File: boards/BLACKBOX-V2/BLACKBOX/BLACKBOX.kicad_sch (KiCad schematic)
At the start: 23 parts, among them J1 Micro_SD_Card, J2 Conn_01x02_Female, U2 Adafruit-BNO085, U4 MS5611-01BA

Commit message: Preliminary layout complete
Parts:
- removed D1: BLUE, symbol Simulation_SPICE:DIODE
- removed D2: RED, symbol Simulation_SPICE:DIODE
- added D103: BLUE, LED_SMD:LED_0805_2012Metric, symbol Device:LED
- added D104: RED, LED_SMD:LED_0805_2012Metric, symbol Device:LED
- R103: renamed from R5; value 10kΩ -> 10k
- R104: renamed from R6; value 10kΩ -> 10k
- R105: renamed from R3; footprint (none) -> Resistor_SMD:R_0805_2012Metric
- R106: renamed from R4; footprint (none) -> Resistor_SMD:R_0805_2012Metric
- gave numbers to parts that had none: 4
- renumbered A1 to A101, C2 to C101, C6 to C104, D3 to D101, D4 to D102, J1 to J101, J2 to J102, JP1 to JP102, JP3 to JP103, R1 to R101, R2 to R102, U2 to U101, U4 to U103
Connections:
- net 3V3 is gone; now on net +3V3: JP101.1
- net KX122_CS is gone; now on net KX_CS: U102.10 (~{CS})
- net KX122_INT1 is gone; now on net KX_INT1: U102.5 (INT1)
- net KX122_INT2 is gone; now on net KX_INT2: U102.6 (INT2)
- net SNS_SPI_MISO is gone; now on net MISO: U102.1 (SDO/ADDR)
- net SNS_SPI_MOSI is gone; now on net MOSI: U102.2 (SDI/SDA)
- net SNS_SPI_SCK is gone; now on net SCK: U102.12 (SCLK/SCL)
- net LED2: now also D103.2 (A)
- net LED3: now also D104.2 (A)
- net at R106.1: now also D104.1 (K)
- net at R105.1: now also D103.1 (K)
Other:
- note added: "LEDs"
- moved on the sheet: D101, D102, R103, R104, R105, R106

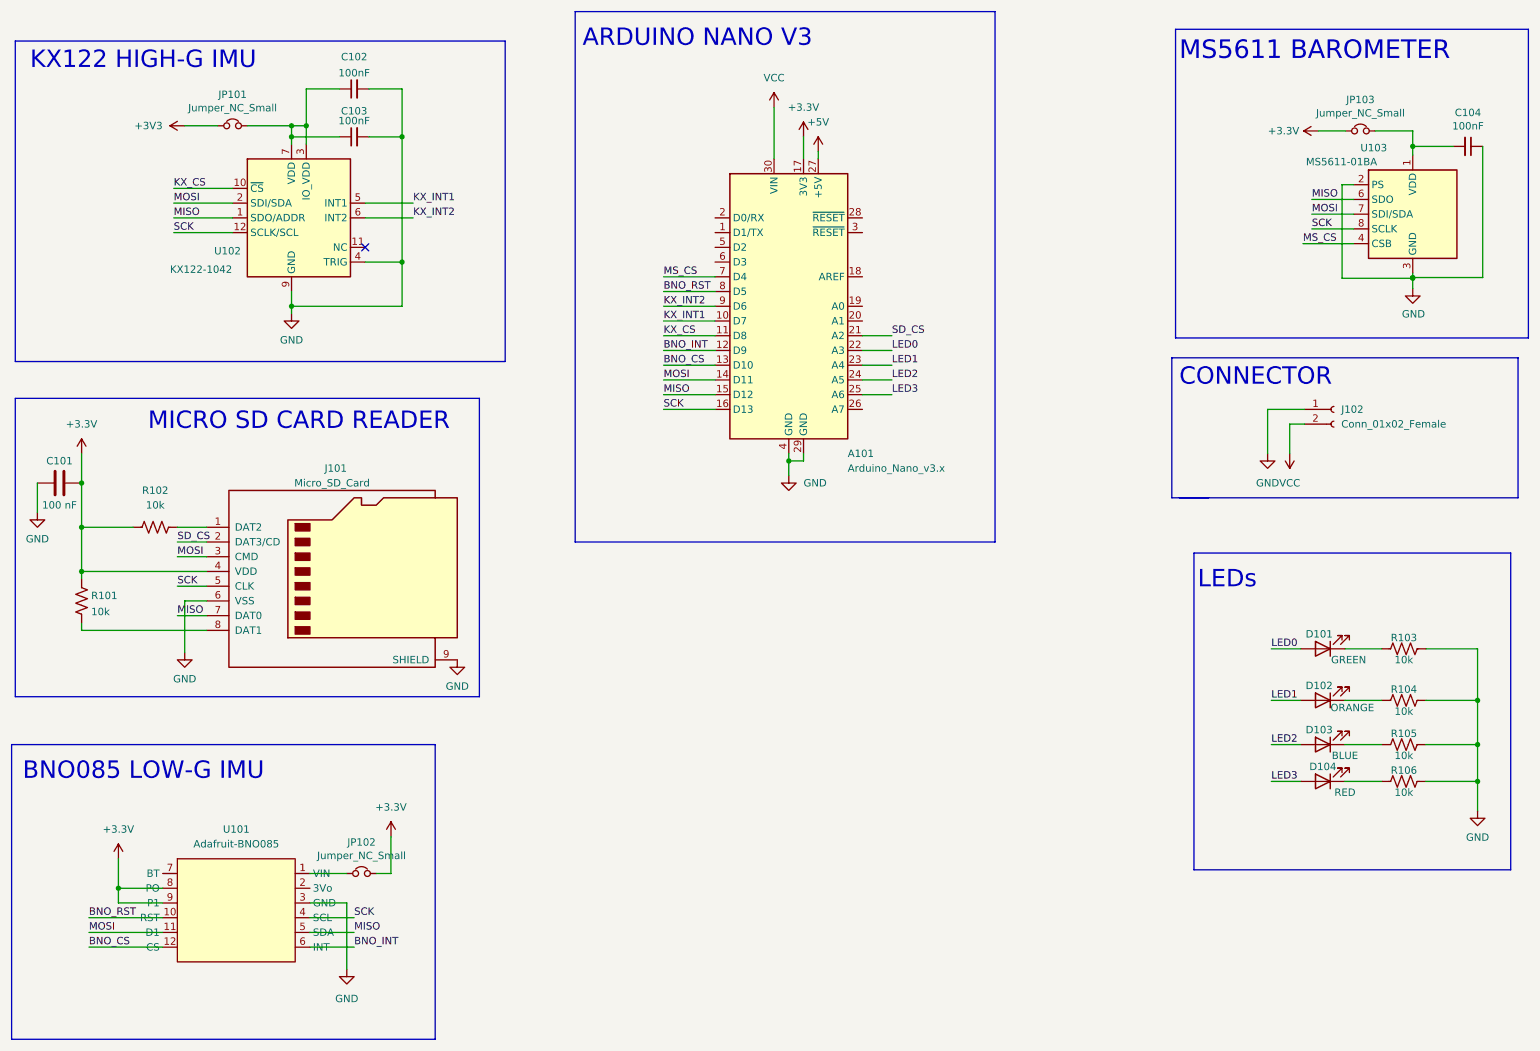
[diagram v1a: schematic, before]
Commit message: finished blackbox routing;
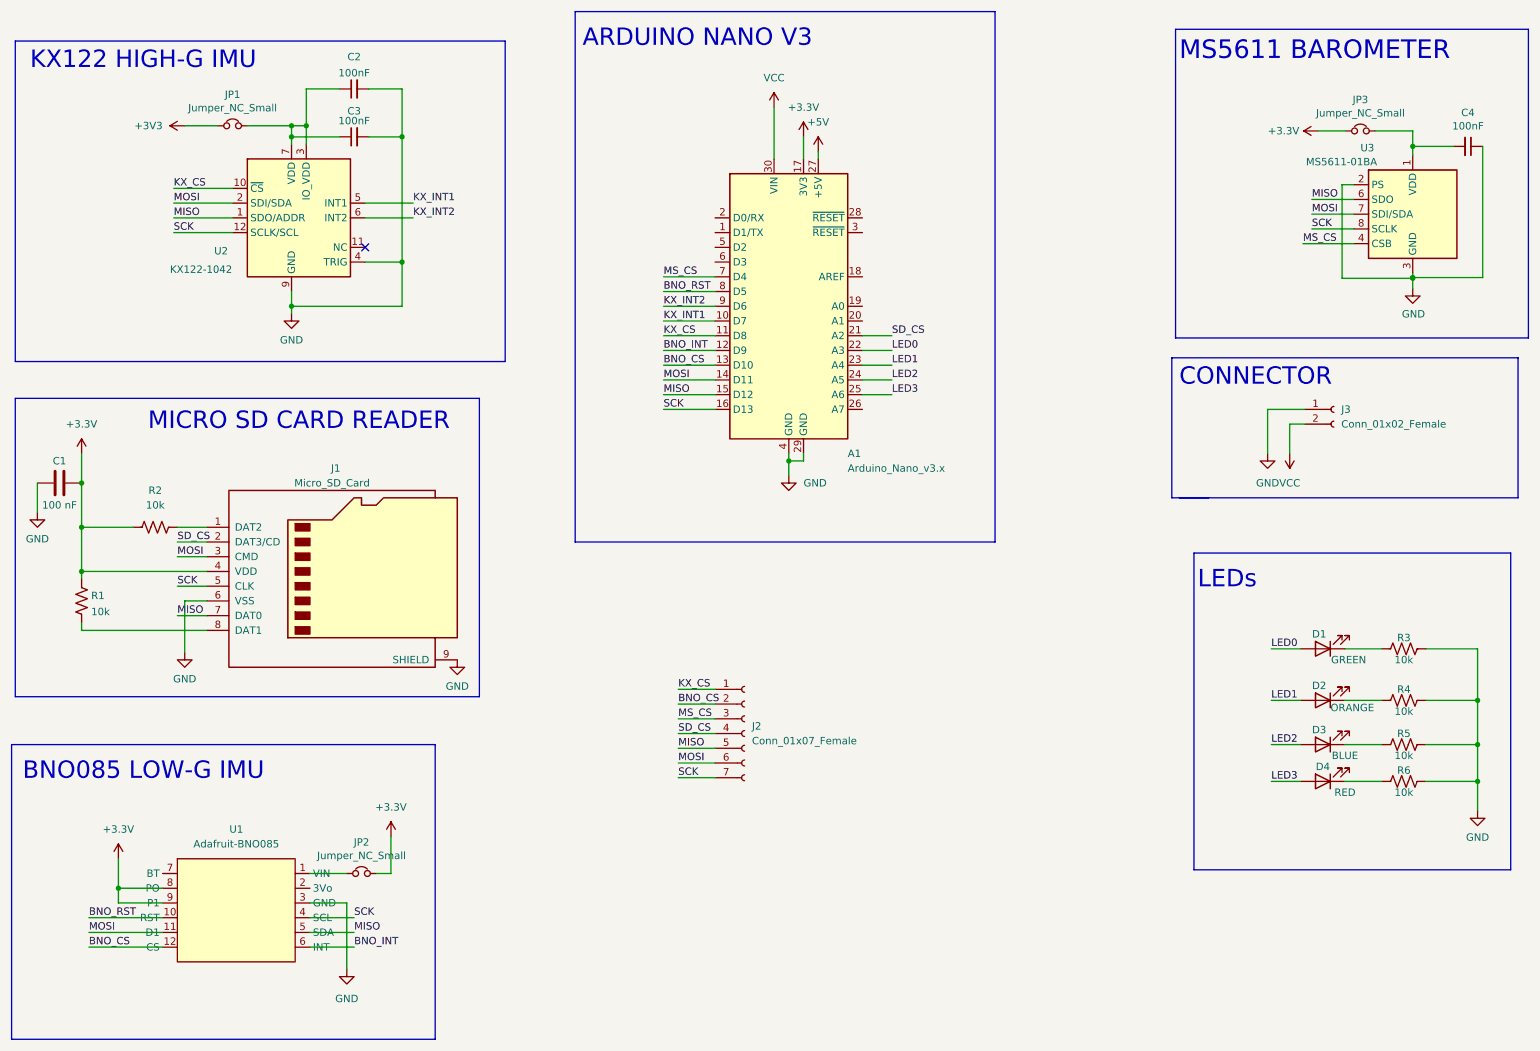
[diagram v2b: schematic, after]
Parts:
- added J2: Conn_01x07_Female, Connector_PinHeader_2.54mm:PinHeader_1x07_P2.54mm_Vertical, symbol Connector:Conn_01x07_Female
- renumbered A101 to A1, C101 to C1, C102 to C2, C103 to C3, C104 to C4, D101 to D1, D102 to D2, D103 to D3, D104 to D4, J101 to J1, J102 to J3, JP101 to JP1, JP102 to JP2, JP103 to JP3, R101 to R1, R102 to R2, R103 to R3, R104 to R4, R105 to R5, R106 to R6, U101 to U1, U102 to U2, U103 to U3
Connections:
- net BNO_CS: now also J2.2 (Pin_2)
- net KX_CS: now also J2.1 (Pin_1)
- net MISO: now also J2.5 (Pin_5)
- net MOSI: now also J2.6 (Pin_6)
- net MS_CS: now also J2.3 (Pin_3)
- net SCK: now also J2.7 (Pin_7)
- net SD_CS: now also J2.4 (Pin_4)

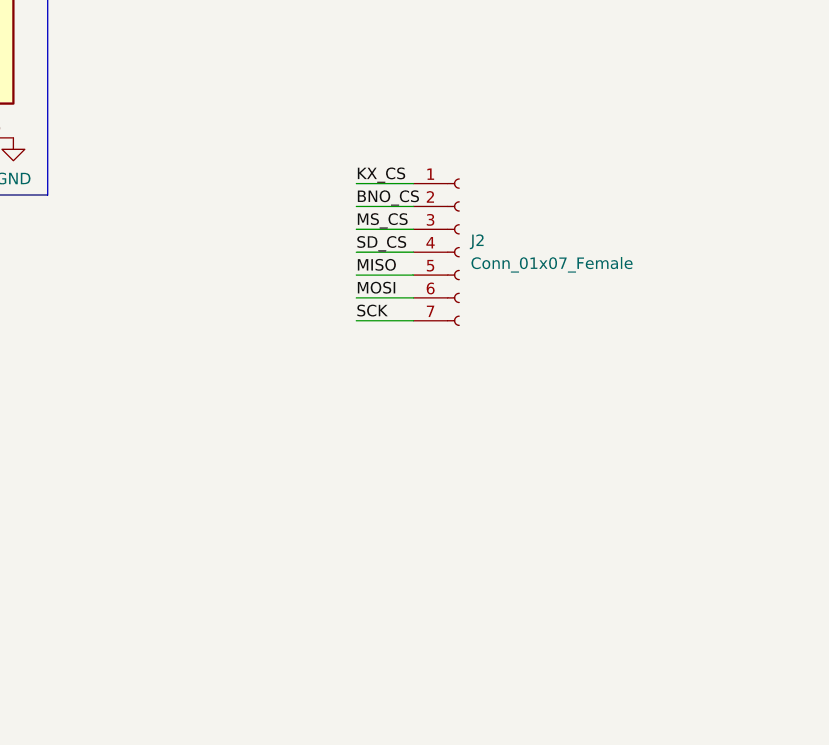
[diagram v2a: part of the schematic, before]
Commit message: Updated schematic for better readability
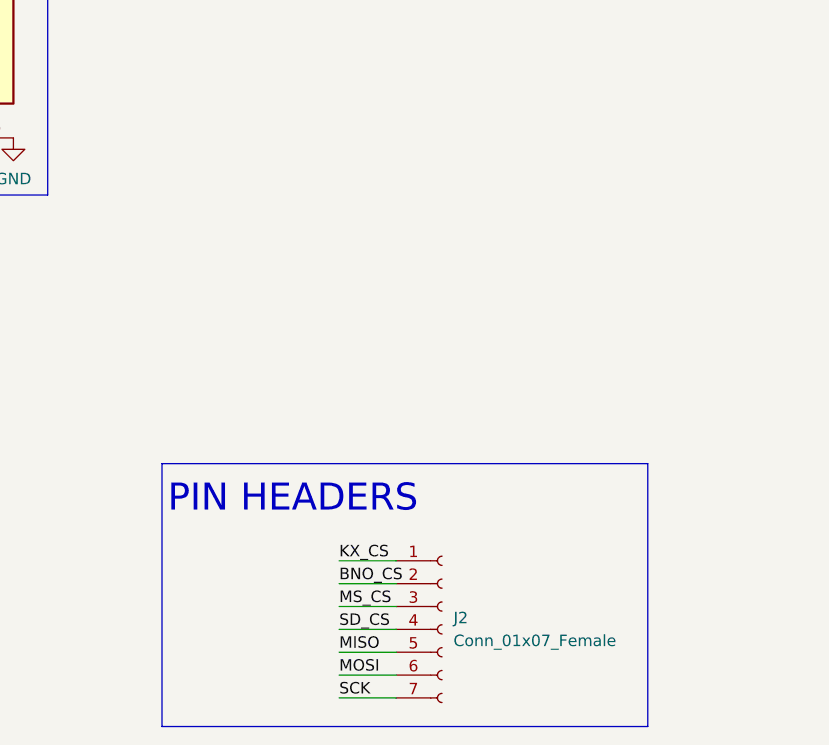
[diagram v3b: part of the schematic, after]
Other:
- note added: "PIN HEADERS"
- moved on the sheet: J2
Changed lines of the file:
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@@
     (stroke (width 0) (type default) (color 0 0 0 0))
   )
-  (wire (pts (xy 134.62 144.78) (xy 140.97 144.78))
+  (wire (pts (xy 132.715 186.69) (xy 139.065 186.69))
     (stroke (width 0) (type default) (color 0 0 0 0))
   )
@@
     (stroke (width 0) (type default) (color 0 0 0 0))
   )
-  (wire (pts (xy 134.62 137.16) (xy 140.97 137.16))
+  (wire (pts (xy 132.715 179.07) (xy 139.065 179.07))
     (stroke (width 0) (type default) (color 0 0 0 0))
   )
@@
     (stroke (width 0) (type default) (color 0 0 0 0))
   )
-  (wire (pts (xy 134.62 132.08) (xy 140.97 132.08))
-    (stroke (width 0) (type default) (color 0 0 0 0))
-  )
-  (wire (pts (xy 134.62 142.24) (xy 140.97 142.24))
+  (wire (pts (xy 132.715 173.99) (xy 139.065 173.99))
+    (stroke (width 0) (type default) (color 0 0 0 0))
+  )
+  (wire (pts (xy 132.715 184.15) (xy 139.065 184.15))
     (stroke (width 0) (type default) (color 0 0 0 0))
   )
@@
     (stroke (width 0) (type default) (color 0 0 0 0))
   )
-  (wire (pts (xy 134.62 139.7) (xy 140.97 139.7))
+  (wire (pts (xy 132.715 181.61) (xy 139.065 181.61))
     (stroke (width 0) (type default) (color 0 0 0 0))
   )
@@
     (stroke (width 0) (type default) (color 0 0 0 0))
   )
+  (polyline (pts (xy 113.03 160.655) (xy 167.005 160.655))
+    (stroke (width 0) (type default) (color 0 0 0 0))
+  )
   (polyline (pts (xy 92.71 189.865) (xy 19.685 189.865))
     (stroke (width 0) (type default) (color 0 0 0 0))
   )
+  (polyline (pts (xy 113.03 189.865) (xy 167.005 189.865))
+    (stroke (width 0) (type default) (color 0 0 0 0))
+  )
   (wire (pts (xy 67.945 60.96) (xy 67.945 63.5))
     (stroke (width 0) (type default) (color 0 0 0 0))
@@
     (stroke (width 0) (type default) (color 0 0 0 0))
   )
+  (polyline (pts (xy 167.005 189.865) (xy 167.005 160.655))
+    (stroke (width 0) (type default) (color 0 0 0 0))
+  )
   (wire (pts (xy 261.239 57.785) (xy 261.239 58.547))
     (stroke (width 0) (type default) (color 0 0 0 0))
@@
     (stroke (width 0) (type default) (color 0 0 0 0))
   )
+  (polyline (pts (xy 113.03 160.655) (xy 113.03 189.865))
+    (stroke (width 0) (type default) (color 0 0 0 0))
+  )
   (wire (pts (xy 45.72 163.83) (xy 38.1 163.83))
     (stroke (width 0) (type default) (color 0 0 0 0))
@@
     (stroke (width 0) (type default) (color 0 0 0 0))
   )
-  (wire (pts (xy 134.62 134.62) (xy 140.97 134.62))
+  (wire (pts (xy 132.715 176.53) (xy 139.065 176.53))
     (stroke (width 0) (type default) (color 0 0 0 0))
   )
@@
     (stroke (width 0) (type default) (color 0 0 0 0))
   )
-  (wire (pts (xy 134.62 129.54) (xy 140.97 129.54))
+  (wire (pts (xy 132.715 171.45) (xy 139.065 171.45))
     (stroke (width 0) (type default) (color 0 0 0 0))
   )
@@
     (effects (font (size 3.2004 3.2004)) (justify left bottom))
   )
+  (text "PIN HEADERS" (at 113.665 166.37 0)
+    (effects (font (size 3 3)) (justify left bottom))
+  )
   (label "MS_CS" (at 132.08 58.42 0)
     (effects (font (size 1.27 1.27)) (justify left bottom))
@@
     (effects (font (size 1.27 1.27)) (justify left bottom))
   )
-  (label "SCK" (at 134.62 144.78 0)
+  (label "SCK" (at 132.715 186.69 0)
     (effects (font (size 1.27 1.27)) (justify left bottom))
   )
@@
     (effects (font (size 1.27 1.27)) (justify left bottom))
   )
-  (label "MISO" (at 134.62 139.7 0)
+  (label "MISO" (at 132.715 181.61 0)
     (effects (font (size 1.27 1.27)) (justify left bottom))
   )
@@
     (effects (font (size 1.27 1.27)) (justify left bottom))
   )
-  (label "MS_CS" (at 134.62 134.62 0)
+  (label "MS_CS" (at 132.715 176.53 0)
     (effects (font (size 1.27 1.27)) (justify left bottom))
   )
@@
     (effects (font (size 1.27 1.27)) (justify left bottom))
   )
-  (label "KX_CS" (at 134.62 129.54 0)
+  (label "KX_CS" (at 132.715 171.45 0)
     (effects (font (size 1.27 1.27)) (justify left bottom))
   )
@@
     (effects (font (size 1.27 1.27)) (justify left bottom))
   )
-  (label "MOSI" (at 134.62 142.24 0)
+  (label "MOSI" (at 132.715 184.15 0)
     (effects (font (size 1.27 1.27)) (justify left bottom))
   )
@@
     (effects (font (size 1.27 1.27)) (justify left bottom))
   )
-  (label "SD_CS" (at 134.62 137.16 0)
+  (label "SD_CS" (at 132.715 179.07 0)
     (effects (font (size 1.27 1.27)) (justify left bottom))
   )
@@
     (effects (font (size 1.27 1.27)) (justify left bottom))
   )
-  (label "BNO_CS" (at 134.62 132.08 0)
+  (label "BNO_CS" (at 132.715 173.99 0)
     (effects (font (size 1.27 1.27)) (justify left bottom))
   )
@@
     (pin "2")
   )
-  (symbol (lib_id "Connector:Conn_01x07_Female") (at 146.05 137.16 0) (unit 1)
+  (symbol (lib_id "Connector:Conn_01x07_Female") (at 144.145 179.07 0) (unit 1)
     (in_bom yes) (on_board yes) (fields_autoplaced)
-    (property "Reference" "J2" (id 0) (at 147.32 135.8899 0)
+    (property "Reference" "J2" (id 0) (at 145.415 177.7999 0)
       (effects (font (size 1.27 1.27)) (justify left))
     )
-    (property "Value" "Conn_01x07_Female" (id 1) (at 147.32 138.4299 0)
+    (property "Value" "Conn_01x07_Female" (id 1) (at 145.415 180.3399 0)
       (effects (font (size 1.27 1.27)) (justify left))
     )
-    (property "Footprint" "Connector_PinHeader_2.54mm:PinHeader_1x07_P2.54mm_Vertical" (id 2) (at 146.05 137.16 0)
-      (effects (font (size 1.27 1.27)) hide)
-    )
-    (property "Datasheet" "~" (id 3) (at 146.05 137.16 0)
-      (effects (font (size 1.27 1.27)) hide)
-    )
+    (property "Footprint" "Connector_PinHeader_2.54mm:PinHeader_1x07_P2.54mm_Vertical" (id 2) (at 144.145 179.07 0)
+      (effects (font (size 1.27 1.27)) hide)
+    )
+    (property "Datasheet" "~" (id 3) (at 144.145 179.07 0)
+      (effects (font (size 1.27 1.27)) hide)
+    )
